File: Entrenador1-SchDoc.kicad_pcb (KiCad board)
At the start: 2 copper layers, 154.9 x 63.5 mm, 41 parts, among them J3 ICSP, J5 CON8, J6 CON8, J7 CON8, J9 3vias, P1 CONN_01X04, P10 CONN_01X04, P4 CONN_01X04, P5 CONN_01X09, P6 USB_B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

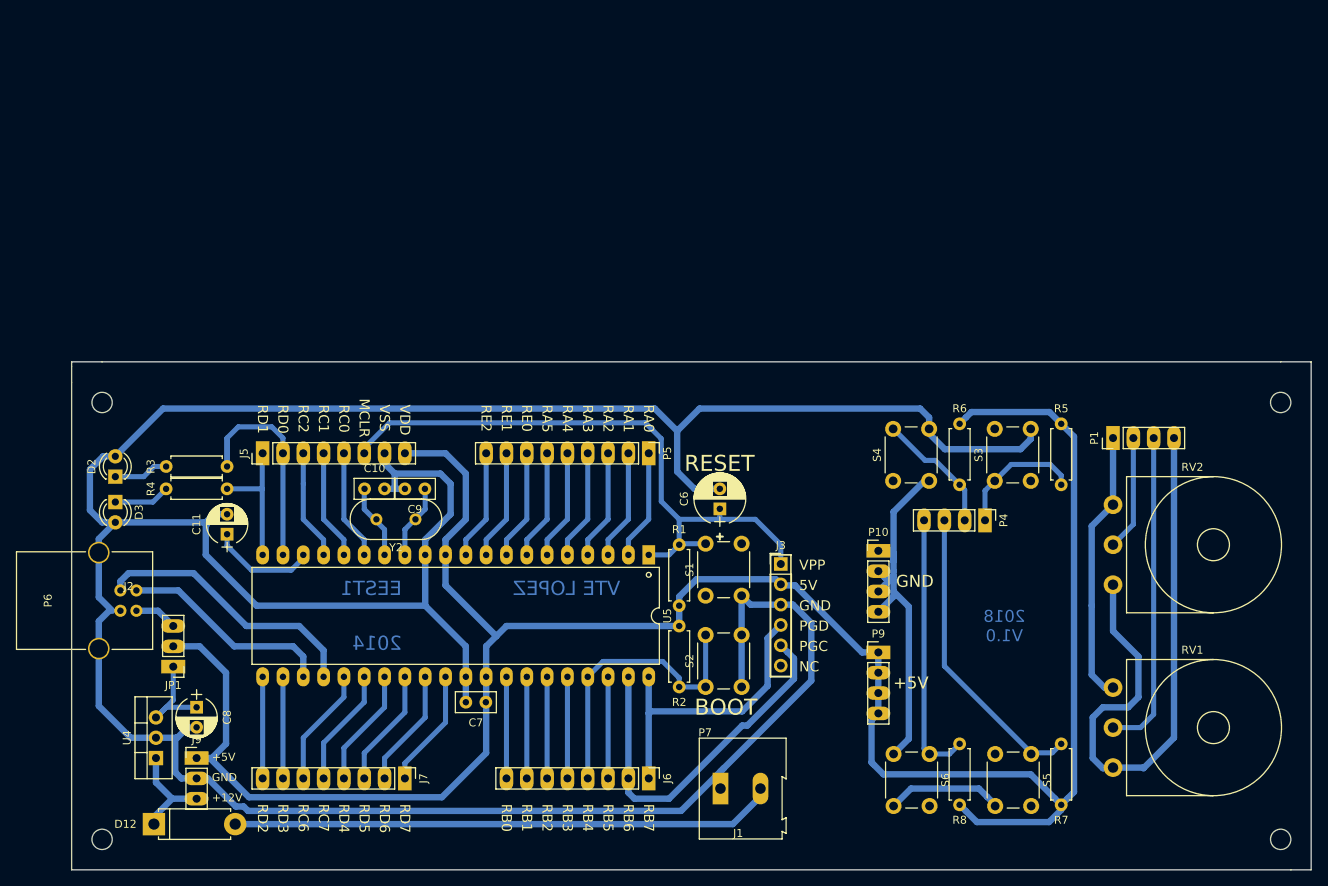
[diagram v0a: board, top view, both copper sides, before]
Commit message: Pequeños ajustes repecto de las capas de información en el PCB
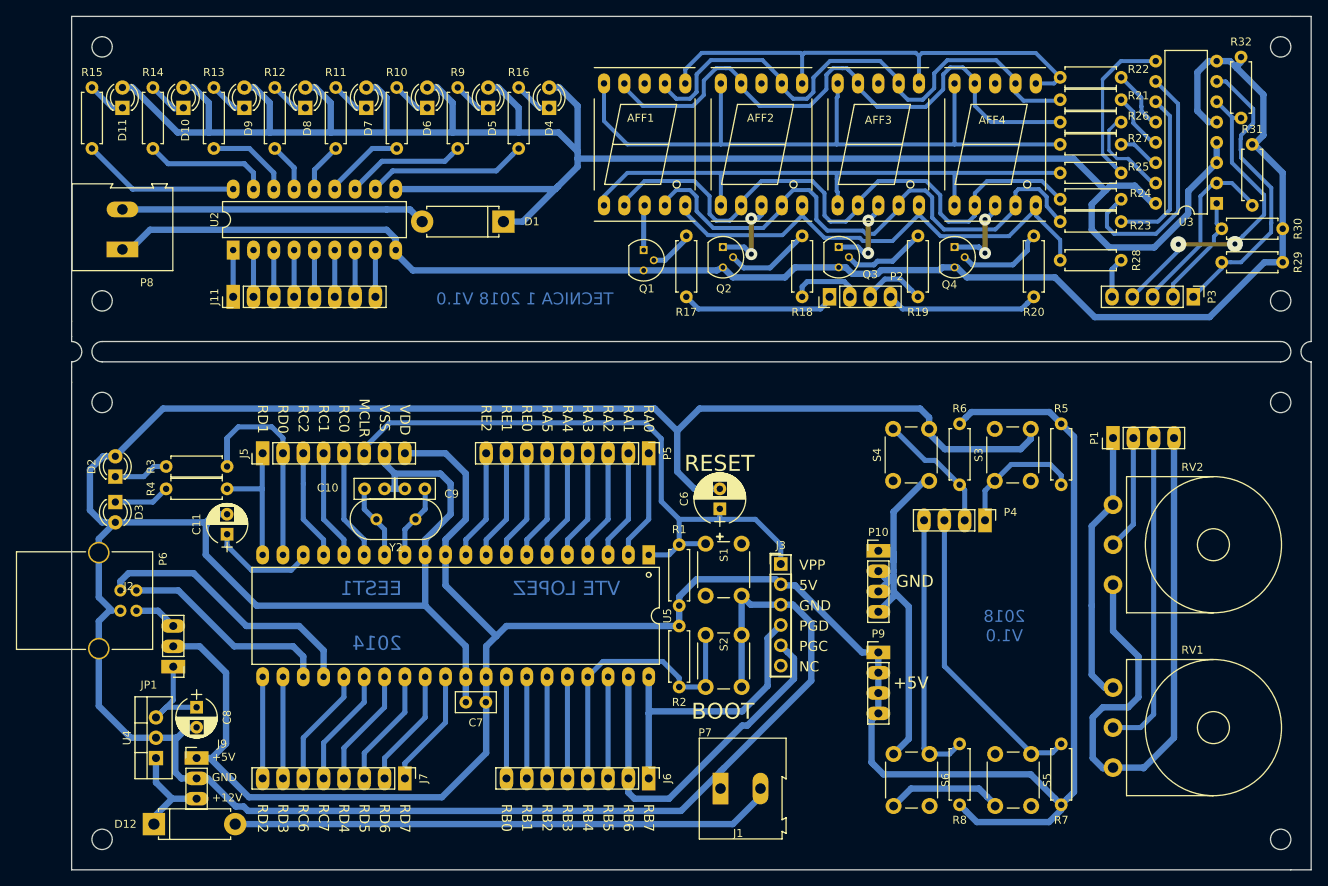
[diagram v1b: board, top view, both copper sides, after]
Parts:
- added AFF1: 7SEGMENTS, libreria:7SegmentLED_LTS6760_LTS6780, F.Cu at (137.7, 49.0)
- added AFF2: 7SEGMENTS, libreria:7SegmentLED_LTS6760_LTS6780, F.Cu at (152.3, 49.0)
- added AFF3: 7SEGMENTS, libreria:7SegmentLED_LTS6760_LTS6780, F.Cu at (166.9, 49.0)
- added AFF4: 7SEGMENTS, libreria:7SegmentLED_LTS6760_LTS6780, F.Cu at (181.5, 49.0)
- added D1: 1n4004, libreria:D_5W_P10.16mm_Horizontal, F.Cu at (120.0, 58.7)
- added D10: LED, libreria:LED_D3.0mm, F.Cu at (80.0, 44.5)
- added D11: LED, libreria:LED_D3.0mm, F.Cu at (72.4, 44.5)
- added D4: LED, libreria:LED_D3.0mm, F.Cu at (125.7, 44.5)
- added D5: LED, libreria:LED_D3.0mm, F.Cu at (118.1, 44.5)
- added D6: LED, libreria:LED_D3.0mm, F.Cu at (110.5, 44.5)
- added D7: LED, libreria:LED_D3.0mm, F.Cu at (102.9, 44.5)
- added D8: LED, libreria:LED_D3.0mm, F.Cu at (95.2, 44.5)
- added D9: LED, libreria:LED_D3.0mm, F.Cu at (87.6, 44.5)
- added J11: CON8, libreria:Socket_Strip_Straight_1x08_Pitch2.54mm, F.Cu at (86.2, 68.1)
- added P2: CONN_01X04, libreria:Socket_Strip_Straight_1x04_Pitch2.54mm, F.Cu at (160.8, 68.1)
- added P3: CONN_01X05, libreria:Socket_Strip_Straight_1x05_Pitch2.54mm, F.Cu at (206.2, 68.1)
- added P8: CONN_01X02, libreria:TerminalBlock_Altech_AK300-2_P5.00mm, F.Cu at (72.4, 62.1)
- added Q1: BC548, TO_SOT_Packages_THT:TO-92_Molded_Narrow, F.Cu at (137.5, 62.2)
- added Q2: BC548, TO_SOT_Packages_THT:TO-92_Molded_Narrow, F.Cu at (147.4, 61.8)
- added Q3: BC548, TO_SOT_Packages_THT:TO-92_Molded_Narrow, F.Cu at (161.9, 61.8)
- added Q4: BC548, TO_SOT_Packages_THT:TO-92_Molded_Narrow, F.Cu at (176.4, 61.8)
- added R10: 180, libreria:R_Axial_DIN0207_L6.3mm_D2.5mm_P7.62mm_Horizontal, F.Cu at (106.7, 41.9)
- added R11: 180, libreria:R_Axial_DIN0207_L6.3mm_D2.5mm_P7.62mm_Horizontal, F.Cu at (99.1, 41.9)
- added R12: 180, libreria:R_Axial_DIN0207_L6.3mm_D2.5mm_P7.62mm_Horizontal, F.Cu at (91.4, 41.9)
- added R13: 180, libreria:R_Axial_DIN0207_L6.3mm_D2.5mm_P7.62mm_Horizontal, F.Cu at (83.8, 41.9)
- added R14: 180, libreria:R_Axial_DIN0207_L6.3mm_D2.5mm_P7.62mm_Horizontal, F.Cu at (76.2, 41.9)
- added R15: 180, libreria:R_Axial_DIN0207_L6.3mm_D2.5mm_P7.62mm_Horizontal, F.Cu at (68.6, 41.9)
- added R16: 180, libreria:R_Axial_DIN0207_L6.3mm_D2.5mm_P7.62mm_Horizontal, F.Cu at (121.9, 41.9)
- added R17: 1200, libreria:R_Axial_DIN0207_L6.3mm_D2.5mm_P7.62mm_Horizontal, F.Cu at (142.9, 68.1)
- added R18: 1200, libreria:R_Axial_DIN0207_L6.3mm_D2.5mm_P7.62mm_Horizontal, F.Cu at (157.4, 68.1)
- added R19: 1200, libreria:R_Axial_DIN0207_L6.3mm_D2.5mm_P7.62mm_Horizontal, F.Cu at (171.8, 68.1)
- added R20: 1200, libreria:R_Axial_DIN0207_L6.3mm_D2.5mm_P7.62mm_Horizontal, F.Cu at (186.3, 68.1)
- added R21: 180, libreria:R_Axial_DIN0207_L6.3mm_D2.5mm_P7.62mm_Horizontal, F.Cu at (197.2, 43.4)
- added R22: 180, libreria:R_Axial_DIN0207_L6.3mm_D2.5mm_P7.62mm_Horizontal, F.Cu at (197.2, 40.6)
- added R23: 180, libreria:R_Axial_DIN0207_L6.3mm_D2.5mm_P7.62mm_Horizontal, F.Cu at (197.2, 58.7)
- added R24: 180, libreria:R_Axial_DIN0207_L6.3mm_D2.5mm_P7.62mm_Horizontal, F.Cu at (197.2, 55.9)
- added R25: 180, libreria:R_Axial_DIN0207_L6.3mm_D2.5mm_P7.62mm_Horizontal, F.Cu at (197.2, 52.6)
- added R26: 180, libreria:R_Axial_DIN0207_L6.3mm_D2.5mm_P7.62mm_Horizontal, F.Cu at (197.2, 46.2)
- added R27: 180, libreria:R_Axial_DIN0207_L6.3mm_D2.5mm_P7.62mm_Horizontal, F.Cu at (197.2, 49.0)
- added R28: 180, libreria:R_Axial_DIN0207_L6.3mm_D2.5mm_P7.62mm_Horizontal, F.Cu at (197.2, 63.5)
- added R29: 10k, libreria:R_Axial_DIN0207_L6.3mm_D2.5mm_P7.62mm_Horizontal, F.Cu at (217.4, 63.8)
- added R30: 10k, libreria:R_Axial_DIN0207_L6.3mm_D2.5mm_P7.62mm_Horizontal, F.Cu at (217.4, 59.6)
- added R31: 10k, libreria:R_Axial_DIN0207_L6.3mm_D2.5mm_P7.62mm_Horizontal, F.Cu at (213.6, 49.0)
- added R32: 10k, libreria:R_Axial_DIN0207_L6.3mm_D2.5mm_P7.62mm_Horizontal, F.Cu at (212.2, 38.1)
- added R9: 180, libreria:R_Axial_DIN0207_L6.3mm_D2.5mm_P7.62mm_Horizontal, F.Cu at (114.3, 41.9)
- added U2: ULN2803, libreria:DIP-18_W7.62mm_LongPads, F.Cu at (86.2, 62.2)
- added U3: 4511, libreria:DIP-16_W7.62mm, F.Cu at (209.2, 56.4)
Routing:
- net VDD: track 284.0 -> 540.8 mm
- net GND: track 470.1 -> 668.8 mm
- net /g: track 0.00 -> 85.8 mm
- net /d: track 0.00 -> 76.6 mm
- net /f: track 0.00 -> 75.0 mm
- net /c: track 0.00 -> 72.1 mm
- net /e: track 0.00 -> 71.4 mm
- net /a: track 0.00 -> 68.5 mm
- net /h: track 0.00 -> 63.6 mm
- net /b: track 0.00 -> 61.7 mm
- net /Display_D: track 0.00 -> 38.9 mm, vias 0 -> 2
- net Net-(D1-Pad2): track 0.00 -> 38.1 mm
- net /Display_A: track 0.00 -> 37.7 mm
- net Net-(R24-Pad1): track 0.00 -> 32.0 mm
- net /Display_C: track 0.00 -> 23.6 mm
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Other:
- board size 154.9 x 63.5 mm -> 154.9 x 106.7 mm
- board text added: "TECNICA 1 2018 V1.0"
